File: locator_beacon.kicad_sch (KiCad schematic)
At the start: 24 parts, among them U5 TL074

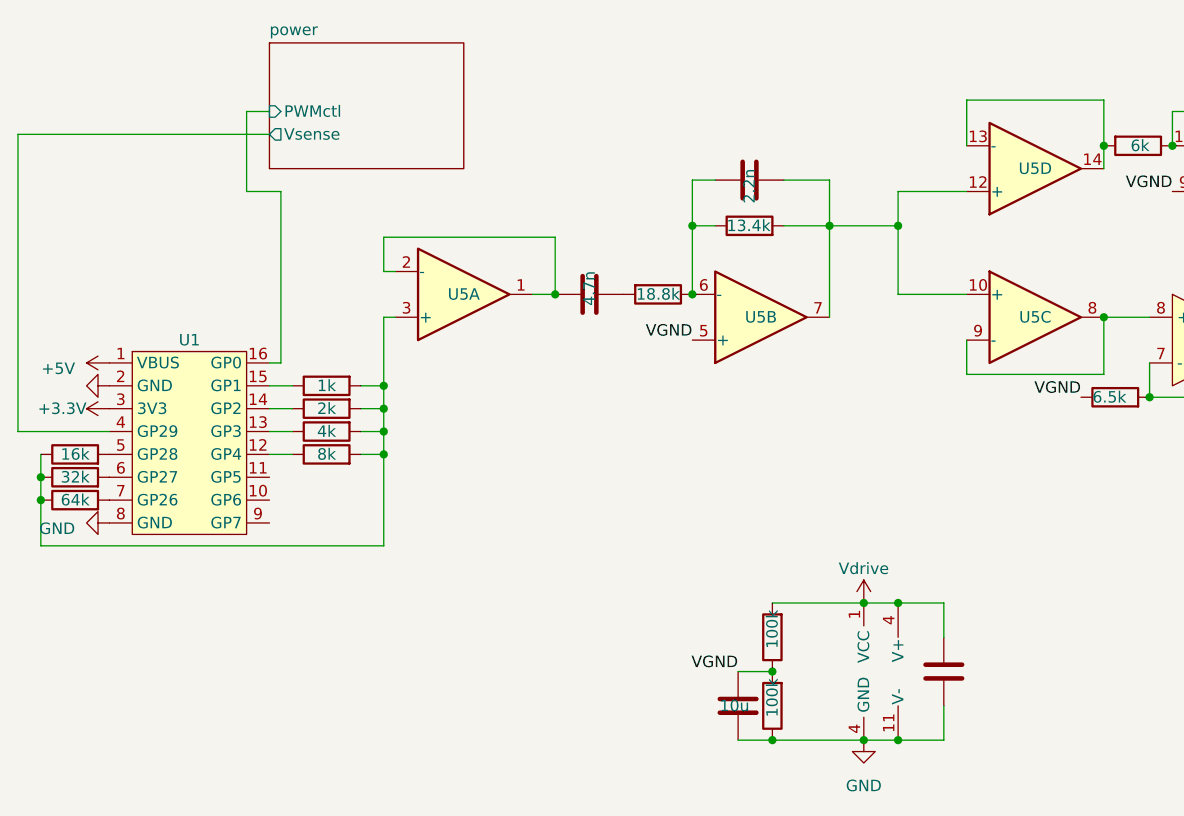
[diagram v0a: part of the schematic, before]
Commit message: Add boost IC
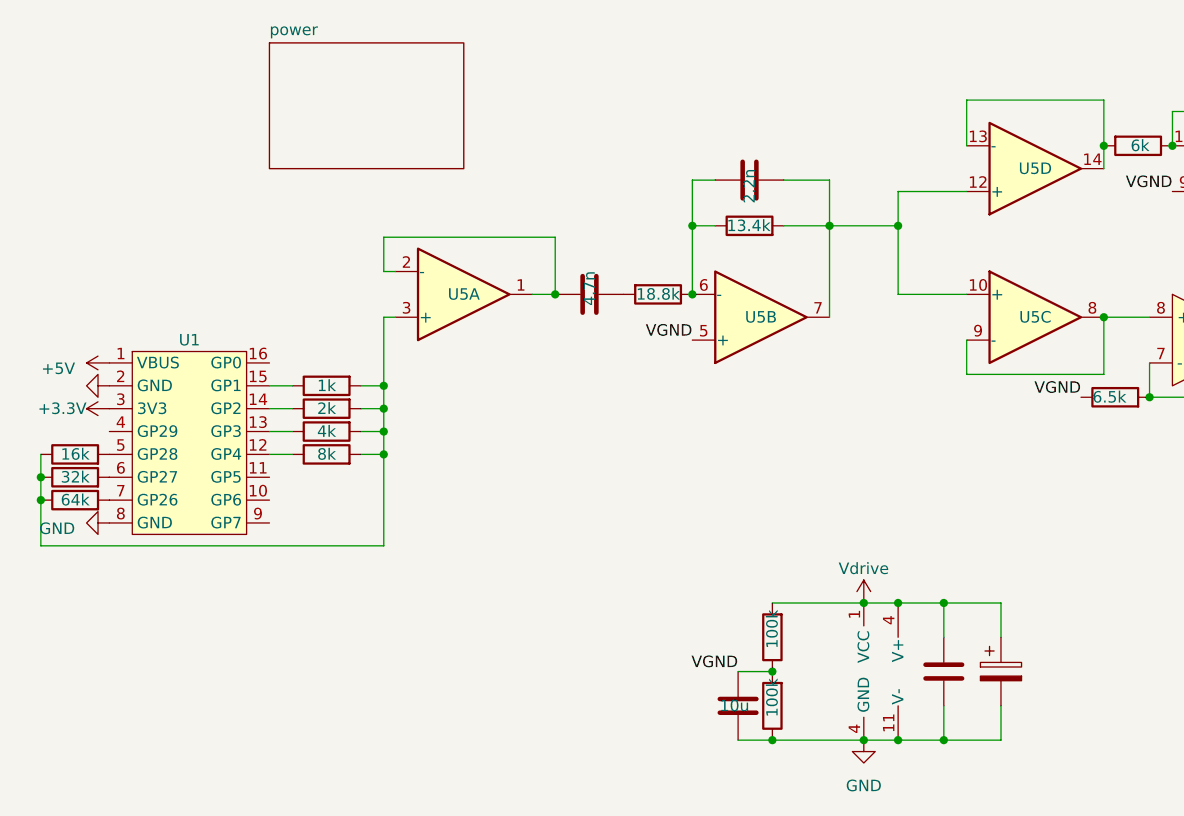
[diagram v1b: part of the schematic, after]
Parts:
- added C1: 4.7uF, Capacitor_THT:CP_Radial_D4.0mm_P2.00mm, symbol Device:C_Polarized
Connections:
- net GND: now also C1.2
- net Vdrive: now also C1.1
- net power/PWMctl: no longer names the net of U1.16 (GP0)
- net power/Vsense: no longer names the net of U1.4 (GP29)
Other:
- sheet power ports: added none; removed PWMctl, Vsense
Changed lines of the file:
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@@
   (junction (at 196.85 99.06) (diameter 0) (color 0 0 0 0)
   )
+  (junction (at 201.93 114.3) (diameter 0) (color 0 0 0 0)
+  )
   (junction (at 219.71 48.26) (diameter 0) (color 0 0 0 0)
   )
@@
   (junction (at 242.57 69.85) (diameter 0) (color 0 0 0 0)
   )
+  (junction (at 201.93 99.06) (diameter 0) (color 0 0 0 0)
+  )
   (junction (at 224.79 76.2) (diameter 0) (color 0 0 0 0)
   )
@@
     (stroke (width 0) (type default))
   )
-  (wire (pts (xy 99.06 80.01) (xy 109.22 80.01))
-    (stroke (width 0) (type default))
-  )
   (wire (pts (xy 156.21 64.77) (xy 158.75 64.77))
     (stroke (width 0) (type default))
@@
     (stroke (width 0) (type default))
   )
-  (wire (pts (xy 128.27 53.34) (xy 124.46 53.34))
-    (stroke (width 0) (type default))
-  )
   (wire (pts (xy 139.7 74.93) (xy 139.7 77.47))
     (stroke (width 0) (type default))
@@
     (stroke (width 0) (type default))
   )
-  (wire (pts (xy 128.27 72.39) (xy 128.27 53.34))
-    (stroke (width 0) (type default))
-  )
   (wire (pts (xy 201.93 102.87) (xy 201.93 99.06))
     (stroke (width 0) (type default))
@@
     (stroke (width 0) (type default))
   )
-  (wire (pts (xy 99.06 46.99) (xy 99.06 80.01))
-    (stroke (width 0) (type default))
-  )
   (wire (pts (xy 173.99 57.15) (xy 173.99 64.77))
     (stroke (width 0) (type default))
@@
     (stroke (width 0) (type default))
   )
+  (wire (pts (xy 208.28 114.3) (xy 201.93 114.3))
+    (stroke (width 0) (type default))
+  )
   (wire (pts (xy 224.79 72.39) (xy 224.79 76.2))
     (stroke (width 0) (type default))
@@
     (stroke (width 0) (type default))
   )
-  (wire (pts (xy 124.46 53.34) (xy 124.46 44.45))
-    (stroke (width 0) (type default))
-  )
   (wire (pts (xy 101.6 82.55) (xy 101.6 85.09))
     (stroke (width 0) (type default))
@@
     (stroke (width 0) (type default))
   )
-  (wire (pts (xy 127 72.39) (xy 128.27 72.39))
-    (stroke (width 0) (type default))
-  )
   (wire (pts (xy 179.07 106.68) (xy 182.88 106.68))
     (stroke (width 0) (type default))
@@
     (stroke (width 0) (type default))
   )
+  (wire (pts (xy 208.28 102.87) (xy 208.28 99.06))
+    (stroke (width 0) (type default))
+  )
   (wire (pts (xy 219.71 48.26) (xy 219.71 50.8))
     (stroke (width 0) (type default))
@@
     (stroke (width 0) (type default))
   )
-  (wire (pts (xy 124.46 44.45) (xy 127 44.45))
-    (stroke (width 0) (type default))
-  )
   (wire (pts (xy 196.85 57.15) (xy 196.85 64.77))
     (stroke (width 0) (type default))
@@
     (stroke (width 0) (type default))
   )
+  (wire (pts (xy 208.28 99.06) (xy 201.93 99.06))
+    (stroke (width 0) (type default))
+  )
   (wire (pts (xy 242.57 50.8) (xy 242.57 52.07))
     (stroke (width 0) (type default))
@@
     (stroke (width 0) (type default))
   )
+  (wire (pts (xy 208.28 110.49) (xy 208.28 114.3))
+    (stroke (width 0) (type default))
+  )
   (wire (pts (xy 242.57 63.5) (xy 242.57 59.69))
     (stroke (width 0) (type default))
@@
   )
   (wire (pts (xy 204.47 73.66) (xy 219.71 73.66))
-    (stroke (width 0) (type default))
-  )
-  (wire (pts (xy 127 46.99) (xy 99.06 46.99))
     (stroke (width 0) (type default))
   )
@@
     )
   )
+  (symbol (lib_id "Device:C_Polarized") (at 208.28 106.68 0) (unit 1)
+    (in_bom yes) (on_board yes) (dnp no) (fields_autoplaced)
+    (property "Reference" "C1" (at 212.09 105.156 0)
+      (effects (font (size 1.27 1.27)) (justify left) hide)
+    )
+    (property "Value" "4.7uF" (at 212.09 107.696 0)
+      (effects (font (size 1.27 1.27)) (justify left) hide)
+    )
+    (property "Footprint" "Capacitor_THT:CP_Radial_D4.0mm_P2.00mm" (at 209.2452 110.49 0)
+      (effects (font (size 1.27 1.27)) hide)
+    )
+    (property "Datasheet" "~" (at 208.28 106.68 0)
+      (effects (font (size 1.27 1.27)) hide)
+    )
+    (pin "1")
+    (pin "2")
+    (instances
+      (project "locator_beacon"
+        (path "/2e37f9ca-1f81-48a3-bbbb-9eab5c177622"
+          (reference "C1") (unit 1)
+        )
+        (path "/2e37f9ca-1f81-48a3-bbbb-9eab5c177622/45852106-87c2-4e1d-b1b1-72b985aa268b"
+          (reference "C1") (unit 1)
+        )
+      )
+    )
+  )
   (symbol (lib_name "NCV0372B_2") (lib_id "custom_symbols:NCV0372B") (at 227.33 62.23 0) (unit 1)
     (in_bom yes) (on_board yes) (dnp no)
@@
       (effects (font (size 1.27 1.27)) (justify left top) hide)
     )
-    (pin "PWMctl" input (at 127 44.45 180)
-      (effects (font (size 1.27 1.27)) (justify left))
-    )
-    (pin "Vsense" output (at 127 46.99 180)
-      (effects (font (size 1.27 1.27)) (justify left))
-    )
-    (instances
+    (instances

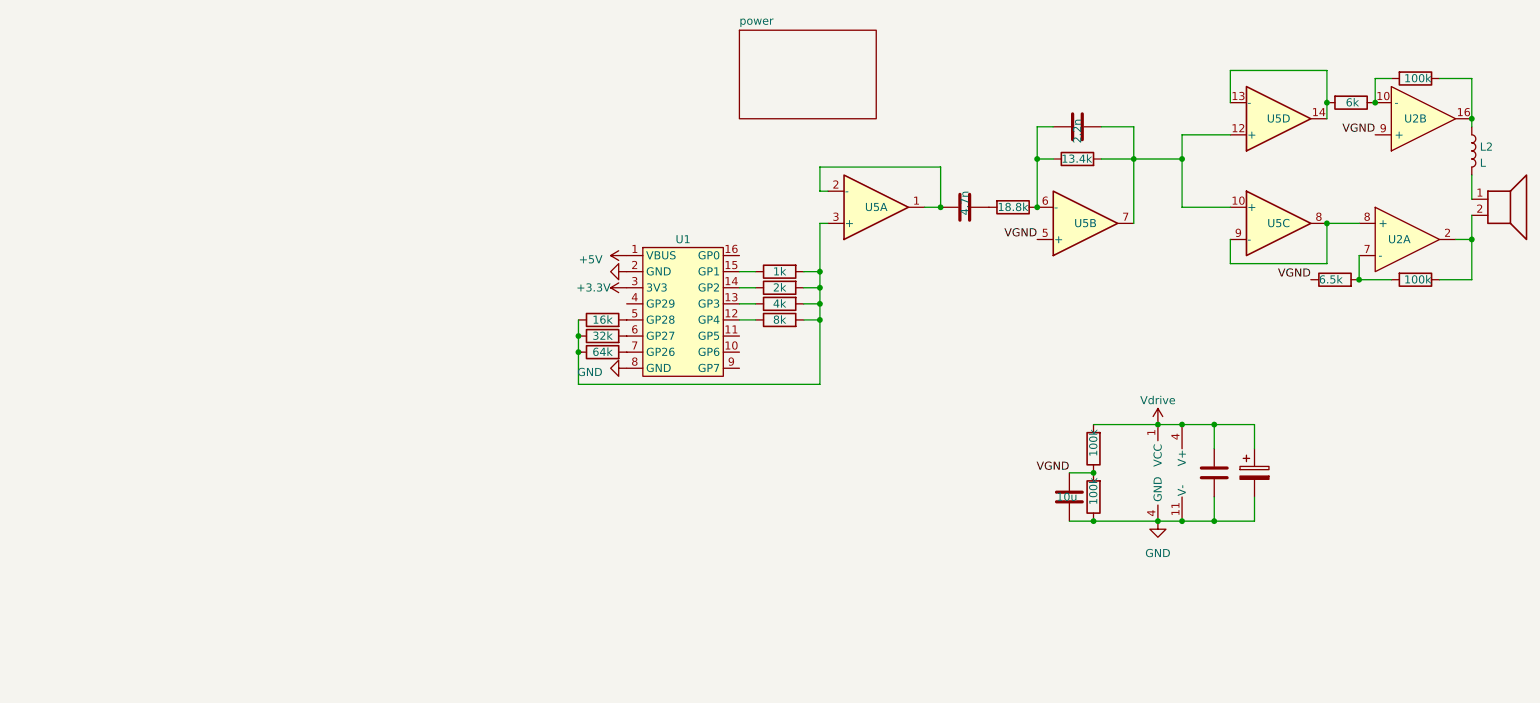
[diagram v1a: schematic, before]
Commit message: First production prototype
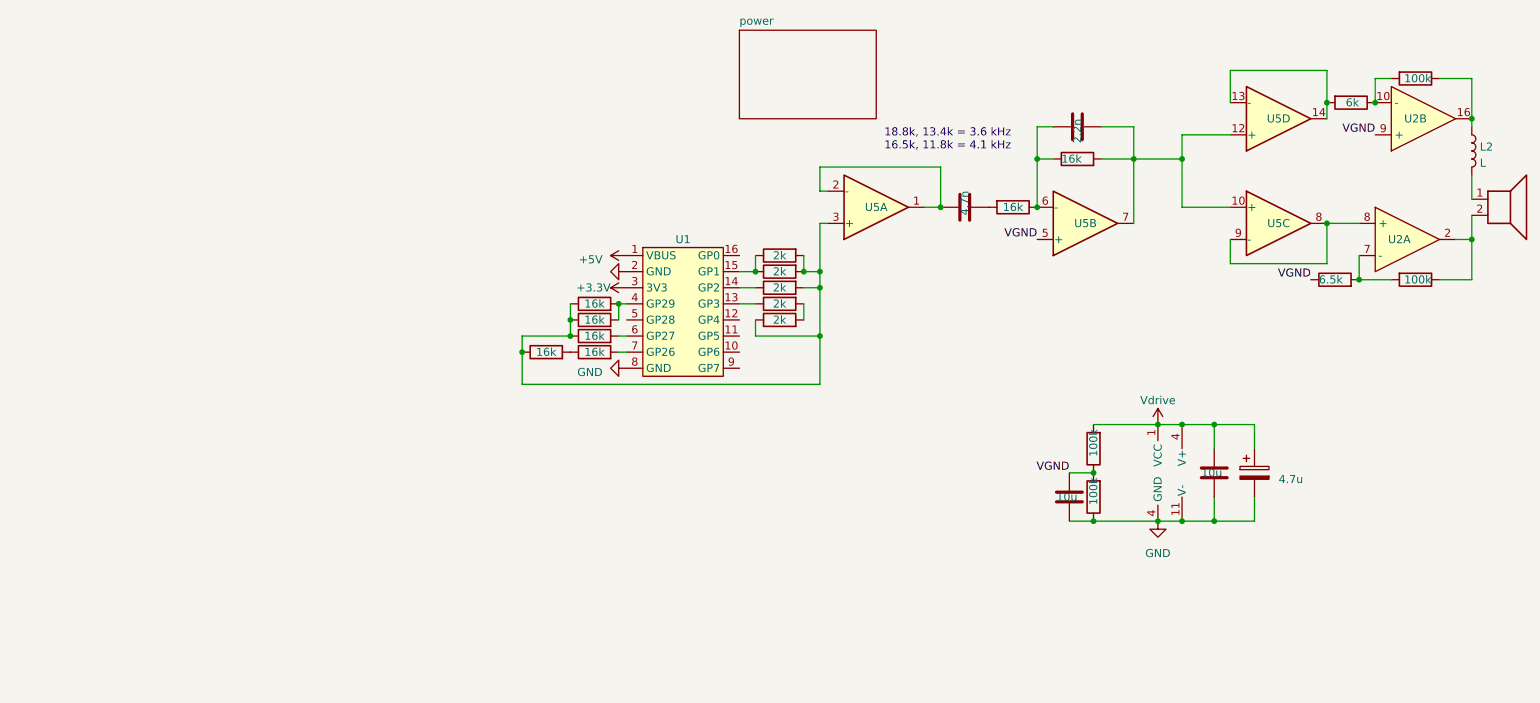
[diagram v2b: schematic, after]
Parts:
- added R12: 2k, Resistor_SMD:R_1206_3216Metric_Pad1.30x1.75mm_HandSolder, symbol Device:R
- added R13, R17: 16k, Resistor_SMD:R_1206_3216Metric_Pad1.30x1.75mm_HandSolder, symbol Device:R
- C1: value 4.7uF -> 4.7u
- C8: value 10n -> 10u
- L2: footprint Inductor_SMD:L_Wuerth_MAPI-3020 -> Inductor_SMD:L_Wuerth_MAPI-4030
- R10: value 1k -> 2k
- R11: value 64k -> 16k
- R20: value 18.8k -> 16k
- R4: value 13.4k -> 16k
- R5: value 32k -> 16k
- R7: value 8k -> 2k
- R8: value 4k -> 2k
- U2: value ~ -> TCA0372
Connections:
- net at R10.2, R5.1, R6.1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: now also R7.1, R12.2, R13.1, R17.1; no longer R11.1, R7.2, R8.2
- net at R6.2: now also U1.4 (GP29), R13.2; no longer U1.5 (GP28)
- net at U1.12 (GP4): no longer R7.1
- net at R10.1, U1.15 (GP1): now also R12.1
- new net: R11.1, R17.2
- new net: R7.2, R8.2
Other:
- note added: "18.8k, 13.4k = 3.6 kHz 16.5k, 11.8k = 4.1 kHz"

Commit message: Prod 1a
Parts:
- OUT1: footprint Connector_PinHeader_1.27mm:PinHeader_1x02_P1.27mm_Vertical -> Connector_PinSocket_2.54mm:PinSocket_1x02_P2.54mm_Vertical
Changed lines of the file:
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@@
       (effects (font (size 1.27 1.27)) (justify left) hide)
     )
-    (property "Footprint" "Connector_PinHeader_1.27mm:PinHeader_1x02_P1.27mm_Vertical" (at 247.65 68.58 0)
+    (property "Footprint" "Connector_PinSocket_2.54mm:PinSocket_1x02_P2.54mm_Vertical" (at 247.65 68.58 0)
       (effects (font (size 1.27 1.27)) hide)
     )

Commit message: Work
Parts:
- removed C8: 10u, Capacitor_SMD:C_1206_3216Metric_Pad1.33x1.80mm_HandSolder, symbol Device:C
- removed R10, R7, R8, R9: 2k, Resistor_SMD:R_1206_3216Metric_Pad1.30x1.75mm_HandSolder, symbol Device:R
- removed R11, R13, R17, R20, R4, R5, R6: 16k, Resistor_SMD:R_1206_3216Metric_Pad1.30x1.75mm_HandSolder, symbol Device:R
- removed U5: TL074, Package_SO:SOIC-14_3.9x8.7mm_P1.27mm, symbol Amplifier_Operational:TL074
- C7: value 2.2n -> 4.7n
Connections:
- net GND: now also C9.2
- net at C7.1: now also C9.1, R12.2
- net at C7.2: now also R3.2, U2.8 (+)
- net +3.3V: no longer names the net of U1.3 (3V3)
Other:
- moved on the sheet: L2, U2A, U2B

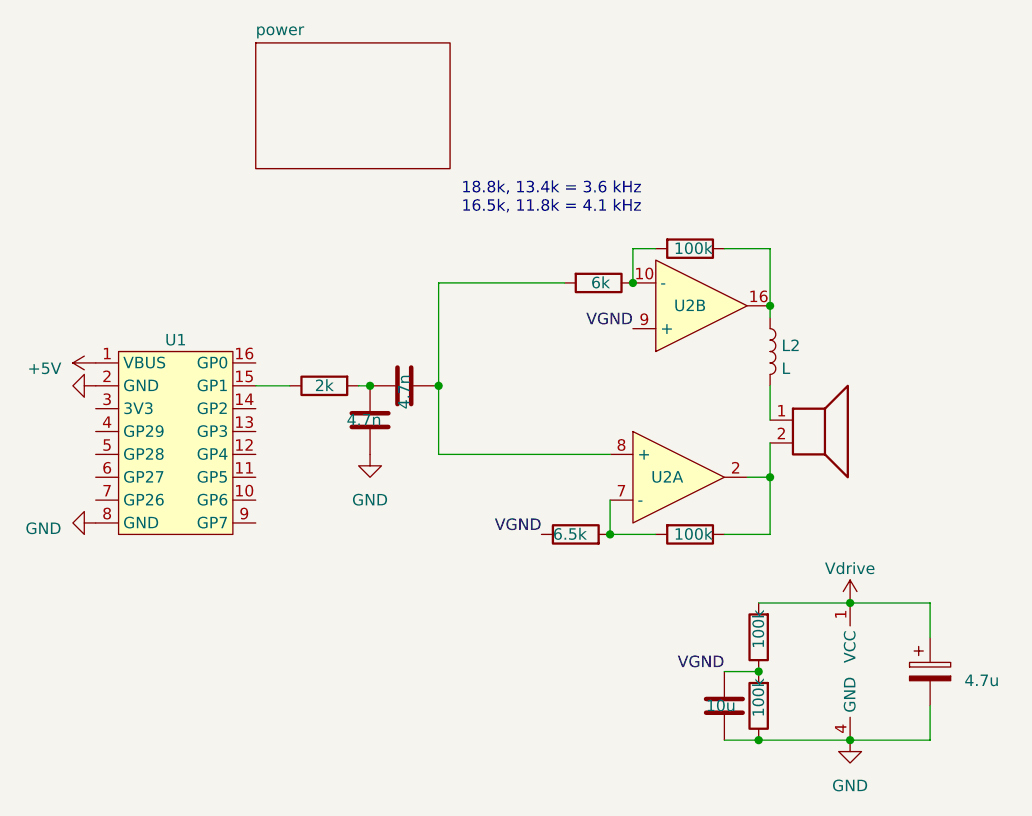
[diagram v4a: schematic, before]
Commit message: Basic Class D amp
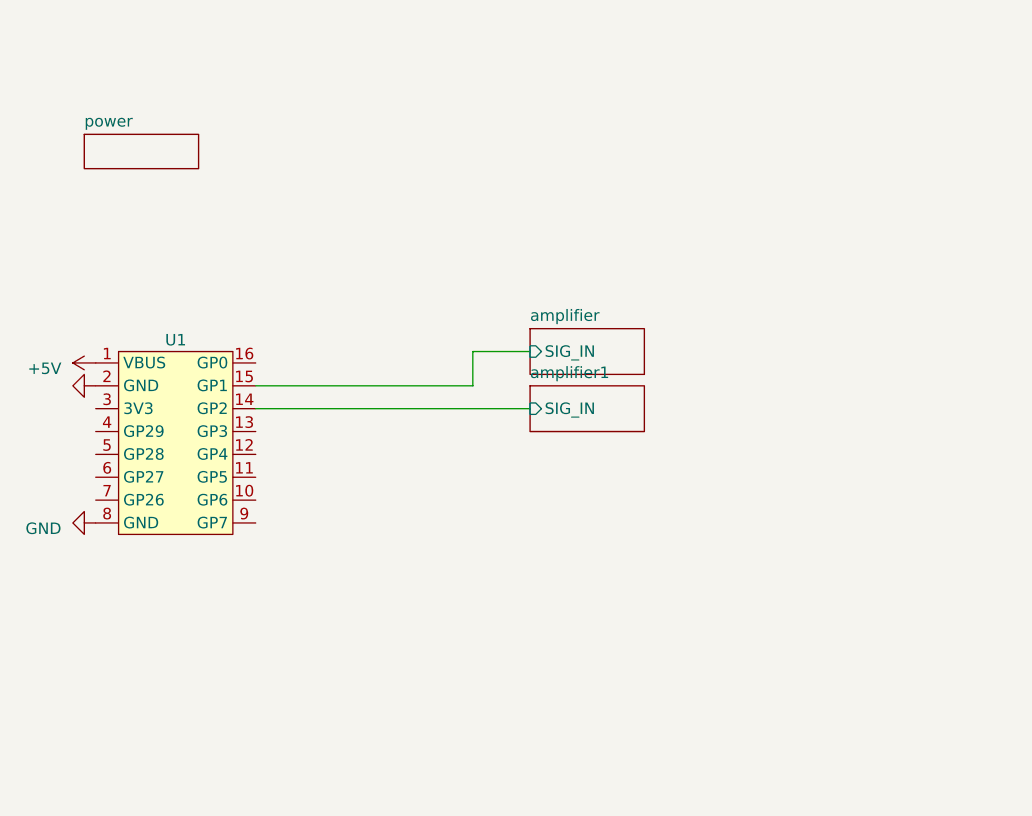
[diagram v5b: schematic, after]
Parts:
- removed C1: 4.7u, Capacitor_THT:CP_Radial_D4.0mm_P2.00mm, symbol Device:C_Polarized
- removed C6: 10u, Capacitor_SMD:C_1206_3216Metric_Pad1.33x1.80mm_HandSolder, symbol Device:C
- removed C7, C9: 4.7n, Capacitor_SMD:C_1206_3216Metric_Pad1.33x1.80mm_HandSolder, symbol Device:C
- removed L2: L, Inductor_SMD:L_Wuerth_MAPI-4030, symbol Device:L
- removed OUT1: Speaker, Connector_PinSocket_2.54mm:PinSocket_1x02_P2.54mm_Vertical, symbol Device:Speaker
- removed R1, R14, R19, R2: 100k, Resistor_SMD:R_1206_3216Metric_Pad1.30x1.75mm_HandSolder, symbol Device:R
- removed R12: 2k, Resistor_SMD:R_1206_3216Metric_Pad1.30x1.75mm_HandSolder, symbol Device:R
- removed R21: 6.5k, Resistor_SMD:R_1206_3216Metric_Pad1.30x1.75mm_HandSolder, symbol Device:R
- removed R3: 6k, Resistor_SMD:R_1206_3216Metric_Pad1.30x1.75mm_HandSolder, symbol Device:R
- removed U2: TCA0372, Package_SO:SOIC-16W_7.5x10.3mm_P1.27mm, symbol custom_symbols:NCV0372B
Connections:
- net amplifier/SIG_IN: now reaches U1.15 (GP1)
- net amplifier1/SIG_IN: now reaches U1.14 (GP2)
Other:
- added sheet amplifier (amplifier.kicad_sch)
- added sheet amplifier1 (amplifier.kicad_sch)
- note removed: "18.8k, 13.4k = 3.6 kHz 16.5k, 11.8k = 4.1 kHz"

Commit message: Seems reasonable
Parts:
- removed U1: ~, RPi:tiny_2040, symbol custom_symbols:tiny_2040
- added J1: Conn_01x02, Connector_PinHeader_2.54mm:PinHeader_1x02_P2.54mm_Horizontal, symbol Connector_Generic:Conn_01x02
- added U13: Pico, custom:rp_pico, symbol MCU_RaspberryPi_and_Boards:Pico
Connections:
- net GND: now also U13.13 (GND), U13.18 (GND), U13.23 (GND), U13.28 (GND), U13.3 (GND), U13.33 (AGND), U13.38 (GND), U13.8 (GND)
- net amplifier/SIG_IN: now also U13.17 (GPIO13)
- new net +BATT: U13.39 (VSYS)
- new net amplifier/OUT_A: J1.2 (Pin_2)
- new net amplifier/OUT_B: J1.1 (Pin_1)
- new net amplifier/~{SIG_IN}: U13.16 (GPIO12)
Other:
- removed sheet amplifier1
- sheet amplifier ports: added OUT_A, OUT_B, ~{SIG_IN}; removed none
